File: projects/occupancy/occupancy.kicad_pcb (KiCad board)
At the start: 2 copper layers, 67 x 61 mm, 16 parts, among them J1 Screw_Terminal_01x02, J2 Conn_01x03_Female, J3 Screw_Terminal_01x02, K1 JQC-3F-1C-DC5V, Q1 BC547, U1 Easy-Power, U2 LM555

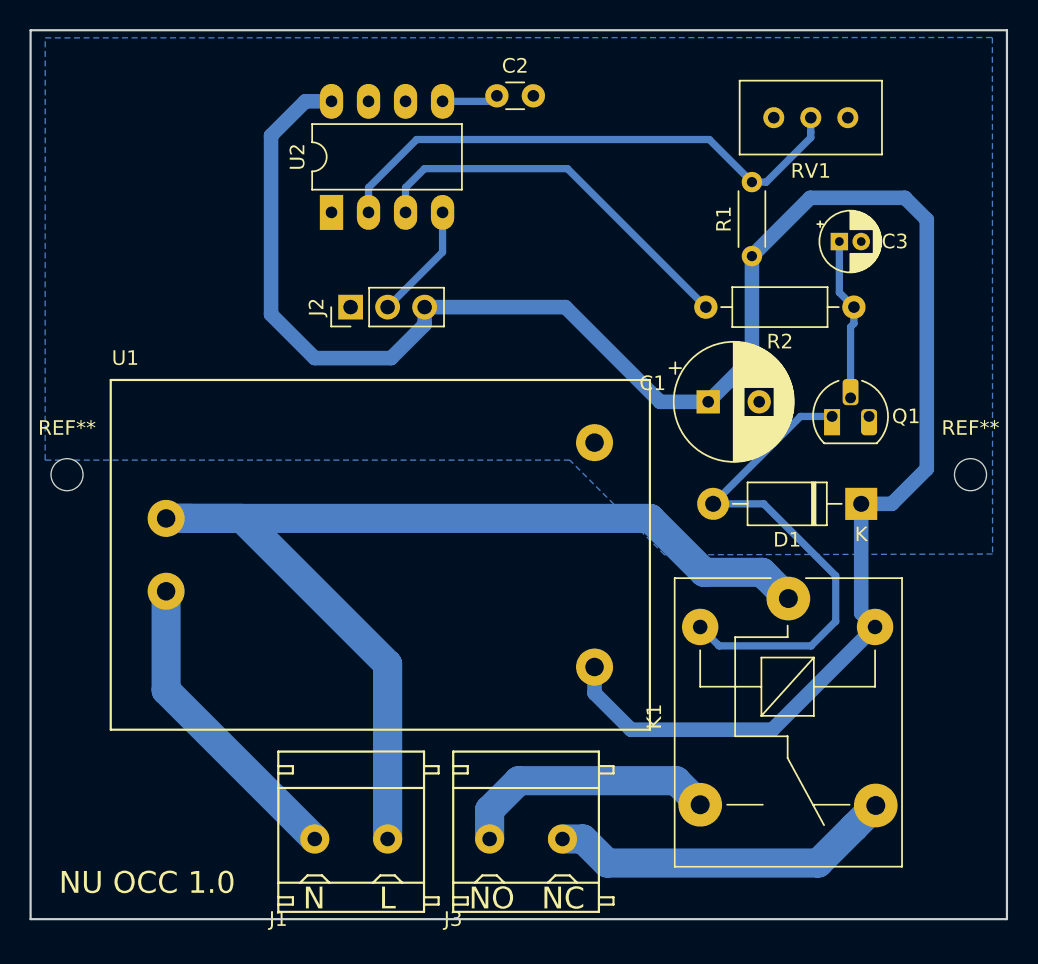
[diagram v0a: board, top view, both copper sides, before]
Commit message: layout wIth the GP box dimensions
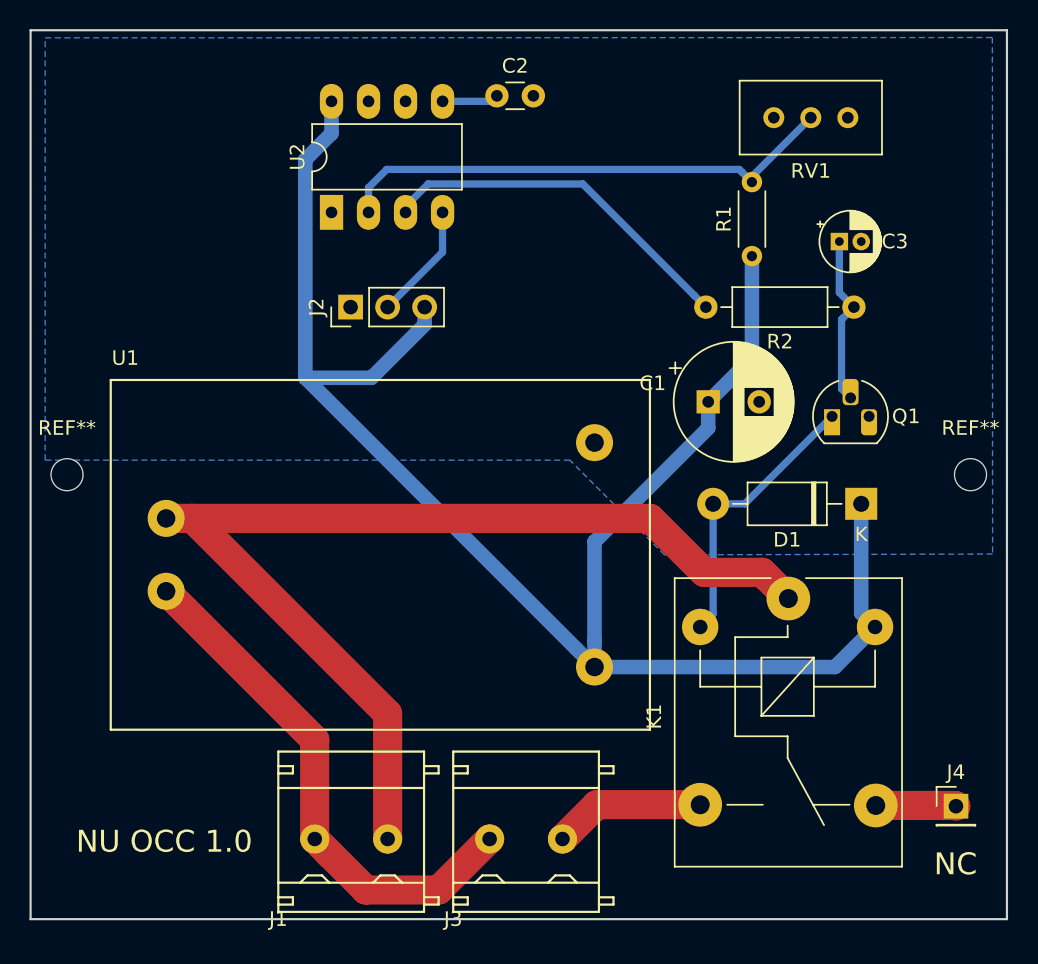
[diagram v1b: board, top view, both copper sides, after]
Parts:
- added J4: Conn_01x01, Connector_PinHeader_2.54mm:PinHeader_1x01_P2.54mm_Vertical, F.Cu at (163.5, 106.2)
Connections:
- J3 pad 1: Net-(J3-Pad1) -> Net-(J1-Pad1)
- K1 pad 3: Net-(J3-Pad1) -> Net-(J3-Pad2)
- K1 pad 4: Net-(J3-Pad2) -> Net-(J4-Pad1)
- RV1 pad 1: Net-(RV1-Pad1) -> (no net)
- U2 pad 7: Net-(U2-Pad7) -> (no net)
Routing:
- net Net-(J3-Pad1): track 18.0 -> 0.00 mm
- net Net-(D1-Pad2): track 34.8 -> 19.5 mm
- net VCC: track 135.8 -> 120.6 mm
- net Net-(J1-Pad1): track 21.2 -> 36.1 mm
- net Net-(J3-Pad2): track 23.8 -> 10.4 mm
- net Net-(J4-Pad1): track 0.00 -> 5.63 mm
- net Net-(J1-Pad2): track 78.1 -> 74.3 mm
- net Net-(R1-Pad2): track 37.3 -> 35.0 mm
- net Net-(R2-Pad2): track 26.8 -> 25.2 mm
- net Net-(C3-Pad1): track 11.2 -> 11.8 mm
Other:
- board text added: "NO-OUT"
- board text removed: "NO"
